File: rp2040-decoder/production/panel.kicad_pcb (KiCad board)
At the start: 4 copper layers, 70 x 70 mm, 535 parts, among them J4 5052702412, Q1 TPM2008, Q2 TPM2008, Q3 TPM2008, Q4 TPM2008, Q5 TPM2008, Q6 TPM2008, Q7 TPM2008, U1 W25Q64JVXGIQ, U2 AP63203WU, U3 RP2040, U4 MD9927, U5 MAX98357A, U6 LMV331, Y1 X252012MMB4SI

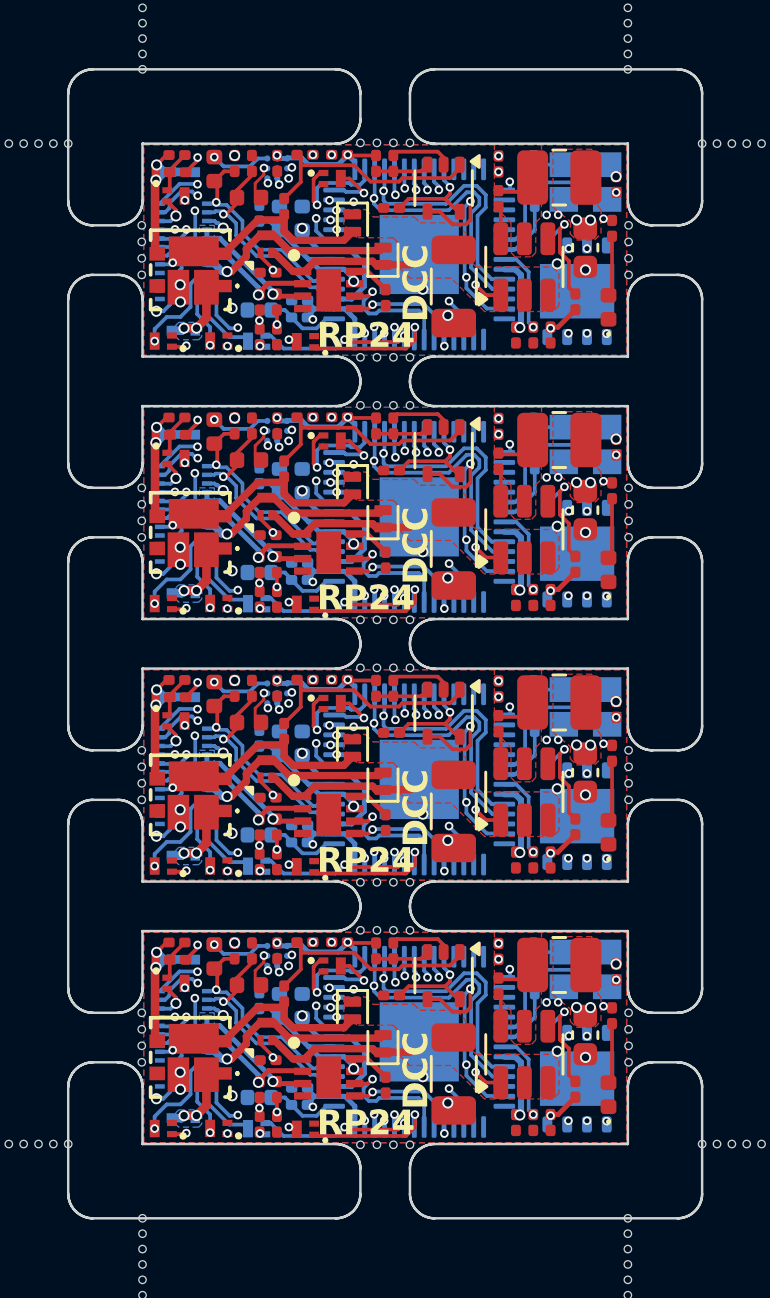
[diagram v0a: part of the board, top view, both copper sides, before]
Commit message: fix: convert 0.2mm vias to 0.3mm
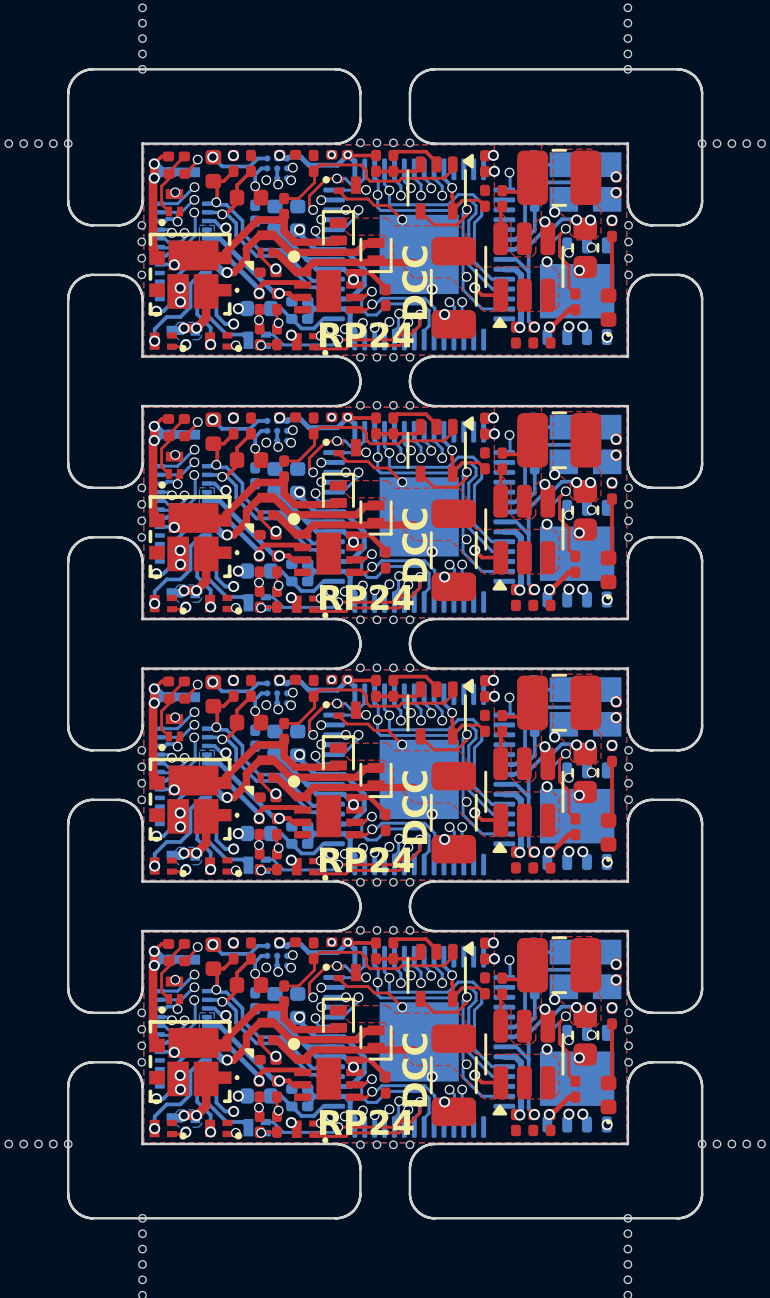
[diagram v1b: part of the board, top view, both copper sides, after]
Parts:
- removed the C10 at (144.2, 37.8)
- removed the C10 at (144.2, 59.0)
- removed the C10 at (144.2, 48.4)
- removed the C10 at (144.2, 69.6)
- removed the C11 at (145.0, 41.1)
- removed the C11 at (145.0, 72.9)
- removed the C11 at (145.0, 62.3)
- removed the C11 at (145.0, 51.7)
- removed the C12 at (143.4, 37.6)
- removed the C12 at (143.4, 58.8)
- removed the C12 at (143.4, 69.4)
- removed the C12 at (143.4, 48.2)
- removed the C14 at (143.4, 52.1)
- removed the C14 at (143.4, 41.5)
- removed the C14 at (143.4, 73.3)
- removed the C14 at (143.4, 62.7)
- removed the C15 at (143.8, 61.2)
- removed the C15 at (143.8, 40.0)
- removed the C15 at (143.8, 50.6)
- removed the C15 at (143.8, 71.8)
- removed the C17 at (153.1, 67.4)
- removed the C17 at (153.1, 35.6)
- removed the C17 at (153.1, 46.2)
- removed the C17 at (153.1, 56.8)
- removed the C18 at (151.3, 40.6)
- removed the C18 at (151.3, 72.4)
- removed the C18 at (151.3, 61.8)
- removed the C18 at (151.3, 51.2)
- removed the C20 at (143.1, 67.4)
- removed the C20 at (143.1, 46.2)
- removed the C20 at (143.1, 35.6)
- removed the C20 at (143.1, 56.8)
- removed the C21 at (144.1, 56.8)
- removed the C21 at (144.1, 67.4)
- removed the C21 at (144.1, 35.6)
- removed the C21 at (144.1, 46.2)
- removed the C22 at (142.4, 67.4)
- removed the C22 at (142.4, 46.2)
- removed the C22 at (142.4, 35.6)
- removed the C22 at (142.4, 56.8)
- removed the C3 at (157.8, 68.2)
- removed the C3 at (157.8, 36.5)
- removed the C3 at (157.8, 47.0)
- removed the C3 at (157.8, 57.6)
- removed the C5 at (148.8, 58.6)
- removed the C5 at (148.8, 37.4)
- removed the C5 at (148.8, 48.0)
- removed the C5 at (148.8, 69.2)
- removed the C6 at (153.1, 37.0)
- removed the C6 at (153.1, 47.6)
- removed the C6 at (153.1, 58.2)
- removed the C6 at (153.1, 68.8)
- removed the C8 at (145.2, 59.0)
- removed the C8 at (145.2, 37.8)
- removed the C8 at (145.2, 69.6)
- removed the C8 at (145.2, 48.4)
- removed the C9 at (156.6, 39.0)
- removed the C9 at (156.6, 49.6)
- removed the C9 at (156.6, 60.2)
- removed the C9 at (156.6, 70.8)
- removed the D1 at (140.6, 39.9)
- removed the D1 at (140.6, 61.1)
- removed the D1 at (140.6, 50.5)
- removed the D1 at (140.6, 71.7)
- removed the D2 at (157.5, 41.4)
- removed the D2 at (157.5, 52.0)
- removed the D2 at (157.5, 62.6)
- removed the D2 at (157.5, 73.2)
- removed the D3 at (148.4, 60.5)
- removed the D3 at (148.4, 39.4)
- removed the D3 at (148.4, 71.2)
- removed the D3 at (148.4, 50.0)
- removed the D4 at (147.2, 59.2)
- removed the D4 at (147.2, 38.0)
- removed the D4 at (147.2, 69.8)
- removed the D4 at (147.2, 48.6)
- removed the FB1 at (141.6, 46.4)
- removed the FB1 at (141.6, 67.6)
- removed the FB1 at (141.6, 35.8)
- removed the FB1 at (141.6, 57.0)
- removed the L1 at (155.5, 68.0)
- removed the L1 at (155.5, 57.4)
- removed the L1 at (155.5, 36.2)
- removed the L1 at (155.5, 46.8)
- removed the Q1 at (140.1, 68.7)
- removed the Q1 at (140.1, 47.5)
- removed the Q1 at (140.1, 58.1)
- removed the Q1 at (140.1, 36.9)
- removed the Q4 at (146.4, 36.2)
- removed the Q4 at (146.4, 68.0)
- removed the Q4 at (146.4, 46.8)
- removed the Q4 at (146.4, 57.4)
- removed the Q5 at (143.3, 53.4)
- removed the Q5 at (143.3, 42.8)
- removed the Q5 at (143.3, 64.0)
- removed the Q5 at (143.3, 74.6)
- removed the R1 at (140.1, 56.5)
- removed the R1 at (140.1, 67.1)
- removed the R1 at (140.1, 35.3)
- removed the R1 at (140.1, 45.9)
- removed the R10 at (145.0, 52.4)
- removed the R10 at (145.0, 41.8)
- removed the R10 at (145.0, 73.6)
- removed the R10 at (145.0, 63.0)
- removed the R11 at (143.4, 51.8)
- removed the R11 at (143.4, 73.0)
- removed the R11 at (143.4, 41.2)
- removed the R11 at (143.4, 62.4)
- removed the R13 at (144.1, 73.0)
- removed the R13 at (144.1, 62.4)
- removed the R13 at (144.1, 51.8)
- removed the R13 at (144.1, 41.2)
- removed the R2 at (140.1, 67.8)
- removed the R2 at (140.1, 46.6)
- removed the R2 at (140.1, 36.0)
- removed the R2 at (140.1, 57.2)
- removed the R4 at (145.3, 56.5)
- removed the R4 at (145.3, 35.2)
- removed the R4 at (145.3, 67.0)
- removed the R4 at (145.3, 45.9)
- removed the R9 at (157.7, 70.0)
- removed the R9 at (157.7, 38.2)
- removed the R9 at (157.7, 59.4)
- removed the R9 at (157.7, 48.8)
- removed the U4 at (146.2, 61.9)
- removed the U4 at (146.2, 40.7)
- removed the U4 at (146.2, 72.5)
- removed the U4 at (146.2, 51.3)
- removed the U6 at (150.9, 47.2)
- removed the U6 at (150.9, 68.4)
- removed the U6 at (150.9, 57.8)
- removed the U6 at (150.9, 36.6)
- added C10: 10uF, Capacitor_SMD:C_0402_1005Metric, B.Cu at (144.1, 69.6)
- added C10: 10uF, Capacitor_SMD:C_0402_1005Metric, B.Cu at (144.1, 59.0)
- added C10: 10uF, Capacitor_SMD:C_0402_1005Metric, B.Cu at (144.1, 48.4)
- added C10: 10uF, Capacitor_SMD:C_0402_1005Metric, B.Cu at (144.1, 37.8)
- added C11: 100nF, Capacitor_SMD:C_0201_0603Metric, B.Cu at (145.1, 51.8)
- added C11: 100nF, Capacitor_SMD:C_0201_0603Metric, B.Cu at (145.1, 41.2)
- added C11: 100nF, Capacitor_SMD:C_0201_0603Metric, B.Cu at (145.1, 62.4)
- added C11: 100nF, Capacitor_SMD:C_0201_0603Metric, B.Cu at (145.1, 73.0)
- added C12: 100nF, Capacitor_SMD:C_0201_0603Metric, B.Cu at (143.2, 69.4)
- added C12: 100nF, Capacitor_SMD:C_0201_0603Metric, B.Cu at (143.2, 48.2)
- added C12: 100nF, Capacitor_SMD:C_0201_0603Metric, B.Cu at (143.2, 58.8)
- added C12: 100nF, Capacitor_SMD:C_0201_0603Metric, B.Cu at (143.2, 37.6)
- added C14: 10uF, Capacitor_SMD:C_0402_1005Metric, B.Cu at (143.4, 41.5)
- added C14: 10uF, Capacitor_SMD:C_0402_1005Metric, B.Cu at (143.4, 62.7)
- added C14: 10uF, Capacitor_SMD:C_0402_1005Metric, B.Cu at (143.4, 52.1)
- added C14: 10uF, Capacitor_SMD:C_0402_1005Metric, B.Cu at (143.4, 73.3)
- added C15: 10pF, Capacitor_SMD:C_0201_0603Metric, F.Cu at (143.8, 50.6)
- added C15: 10pF, Capacitor_SMD:C_0201_0603Metric, F.Cu at (143.8, 61.2)
- added C15: 10pF, Capacitor_SMD:C_0201_0603Metric, F.Cu at (143.8, 40.0)
- added C15: 10pF, Capacitor_SMD:C_0201_0603Metric, F.Cu at (143.8, 71.8)
- added C17: 100nF, Capacitor_SMD:C_0201_0603Metric, F.Cu at (152.5, 67.4)
- added C17: 100nF, Capacitor_SMD:C_0201_0603Metric, F.Cu at (152.5, 35.6)
- added C17: 100nF, Capacitor_SMD:C_0201_0603Metric, F.Cu at (152.5, 46.2)
- added C17: 100nF, Capacitor_SMD:C_0201_0603Metric, F.Cu at (152.5, 56.8)
- added C18: 47uF, Capacitor_SMD:C_1206_3216Metric, F.Cu at (151.3, 72.4)
- added C18: 47uF, Capacitor_SMD:C_1206_3216Metric, F.Cu at (151.3, 40.6)
- added C18: 47uF, Capacitor_SMD:C_1206_3216Metric, F.Cu at (151.3, 51.2)
- added C18: 47uF, Capacitor_SMD:C_1206_3216Metric, F.Cu at (151.3, 61.8)
- added C20: 220pF, Capacitor_SMD:C_0201_0603Metric, F.Cu at (143.1, 46.2)
- added C20: 220pF, Capacitor_SMD:C_0201_0603Metric, F.Cu at (143.1, 35.6)
- added C20: 220pF, Capacitor_SMD:C_0201_0603Metric, F.Cu at (143.1, 56.8)
- added C20: 220pF, Capacitor_SMD:C_0201_0603Metric, F.Cu at (143.1, 67.4)
- added C21: 100nF, Capacitor_SMD:C_0201_0603Metric, F.Cu at (144.6, 45.9)
- added C21: 100nF, Capacitor_SMD:C_0201_0603Metric, F.Cu at (144.6, 56.5)
- added C21: 100nF, Capacitor_SMD:C_0201_0603Metric, F.Cu at (144.6, 67.0)
- added C21: 100nF, Capacitor_SMD:C_0201_0603Metric, F.Cu at (144.6, 35.2)
- added C22: 220pF, Capacitor_SMD:C_0201_0603Metric, F.Cu at (142.4, 67.4)
- added C22: 220pF, Capacitor_SMD:C_0201_0603Metric, F.Cu at (142.4, 56.8)
- added C22: 220pF, Capacitor_SMD:C_0201_0603Metric, F.Cu at (142.4, 35.6)
- added C22: 220pF, Capacitor_SMD:C_0201_0603Metric, F.Cu at (142.4, 46.2)
- added C3: 10pF, Capacitor_SMD:C_0201_0603Metric, F.Cu at (157.8, 68.3)
- added C3: 10pF, Capacitor_SMD:C_0201_0603Metric, F.Cu at (157.8, 36.5)
- added C3: 10pF, Capacitor_SMD:C_0201_0603Metric, F.Cu at (157.8, 57.7)
- added C3: 10pF, Capacitor_SMD:C_0201_0603Metric, F.Cu at (157.8, 47.1)
- added C5: 100nF, Capacitor_SMD:C_0201_0603Metric, F.Cu at (152.5, 37.0)
- added C5: 100nF, Capacitor_SMD:C_0201_0603Metric, F.Cu at (152.5, 68.8)
- added C5: 100nF, Capacitor_SMD:C_0201_0603Metric, F.Cu at (152.5, 58.2)
- added C5: 100nF, Capacitor_SMD:C_0201_0603Metric, F.Cu at (152.5, 47.6)
- added C6: 100nF, Capacitor_SMD:C_0201_0603Metric, F.Cu at (153.2, 37.0)
- added C6: 100nF, Capacitor_SMD:C_0201_0603Metric, F.Cu at (153.2, 58.2)
- added C6: 100nF, Capacitor_SMD:C_0201_0603Metric, F.Cu at (153.2, 68.8)
- added C6: 100nF, Capacitor_SMD:C_0201_0603Metric, F.Cu at (153.2, 47.6)
- added C8: 10uF, Capacitor_SMD:C_0402_1005Metric, B.Cu at (145.0, 37.8)
- added C8: 10uF, Capacitor_SMD:C_0402_1005Metric, B.Cu at (145.0, 59.0)
- added C8: 10uF, Capacitor_SMD:C_0402_1005Metric, B.Cu at (145.0, 48.4)
- added C8: 10uF, Capacitor_SMD:C_0402_1005Metric, B.Cu at (145.0, 69.6)
- added C9: 22uF, Capacitor_SMD:C_0603_1608Metric, F.Cu at (156.6, 70.8)
- added C9: 22uF, Capacitor_SMD:C_0603_1608Metric, F.Cu at (156.6, 60.2)
- added C9: 22uF, Capacitor_SMD:C_0603_1608Metric, F.Cu at (156.6, 49.6)
- added C9: 22uF, Capacitor_SMD:C_0603_1608Metric, F.Cu at (156.6, 39.0)
- added D1: NSR1030QMU, Local Library:NSR1030QMU, F.Cu at (140.6, 40.1)
- added D1: NSR1030QMU, Local Library:NSR1030QMU, F.Cu at (140.6, 61.3)
- added D1: NSR1030QMU, Local Library:NSR1030QMU, F.Cu at (140.6, 50.7)
- added D1: NSR1030QMU, Local Library:NSR1030QMU, F.Cu at (140.6, 71.9)
- added D2: Blue LED, LED_SMD:LED_0402_1005Metric, F.Cu at (157.5, 52.0)
- added D2: Blue LED, LED_SMD:LED_0402_1005Metric, F.Cu at (157.5, 41.4)
- added D2: Blue LED, LED_SMD:LED_0402_1005Metric, F.Cu at (157.5, 62.6)
- added D2: Blue LED, LED_SMD:LED_0402_1005Metric, F.Cu at (157.5, 73.2)
- added D3: PSBD2FD40V1H, Diode_SMD:D_SOD-882, F.Cu at (148.1, 71.0)
- added D3: PSBD2FD40V1H, Diode_SMD:D_SOD-882, F.Cu at (148.1, 60.4)
- added D3: PSBD2FD40V1H, Diode_SMD:D_SOD-882, F.Cu at (148.1, 39.2)
- added D3: PSBD2FD40V1H, Diode_SMD:D_SOD-882, F.Cu at (148.1, 49.8)
- added D4: PSBD2FD40V1H, Diode_SMD:D_SOD-882, F.Cu at (146.6, 38.4)
- added D4: PSBD2FD40V1H, Diode_SMD:D_SOD-882, F.Cu at (146.6, 59.6)
- added D4: PSBD2FD40V1H, Diode_SMD:D_SOD-882, F.Cu at (146.6, 49.0)
- added D4: PSBD2FD40V1H, Diode_SMD:D_SOD-882, F.Cu at (146.6, 70.2)
- added FB1: FB_P, Inductor_SMD:L_0402_1005Metric, F.Cu at (141.6, 57.0)
- added FB1: FB_P, Inductor_SMD:L_0402_1005Metric, F.Cu at (141.6, 67.6)
- added FB1: FB_P, Inductor_SMD:L_0402_1005Metric, F.Cu at (141.6, 46.4)
- added FB1: FB_P, Inductor_SMD:L_0402_1005Metric, F.Cu at (141.6, 35.8)
- added L1: 4.7uH, Inductor_SMD:L_1008_2520Metric, F.Cu at (155.5, 36.2)
- added L1: 4.7uH, Inductor_SMD:L_1008_2520Metric, F.Cu at (155.5, 68.0)
- added L1: 4.7uH, Inductor_SMD:L_1008_2520Metric, F.Cu at (155.5, 57.4)
- added L1: 4.7uH, Inductor_SMD:L_1008_2520Metric, F.Cu at (155.5, 46.8)
- added Q1: TPM2008, Local Library:Diodes_DFN1006-3, F.Cu at (140.0, 58.4)
- added Q1: TPM2008, Local Library:Diodes_DFN1006-3, F.Cu at (140.0, 37.2)
- added Q1: TPM2008, Local Library:Diodes_DFN1006-3, F.Cu at (140.0, 69.0)
- added Q1: TPM2008, Local Library:Diodes_DFN1006-3, F.Cu at (140.0, 47.8)
- added Q4: TPM2008, Local Library:Diodes_DFN1006-3, F.Cu at (147.0, 57.7)
- added Q4: TPM2008, Local Library:Diodes_DFN1006-3, F.Cu at (147.0, 68.3)
- added Q4: TPM2008, Local Library:Diodes_DFN1006-3, F.Cu at (147.0, 47.1)
- added Q4: TPM2008, Local Library:Diodes_DFN1006-3, F.Cu at (147.0, 36.5)
- added Q5: TPM2008, Local Library:Diodes_DFN1006-3, B.Cu at (143.3, 53.3)
- added Q5: TPM2008, Local Library:Diodes_DFN1006-3, B.Cu at (143.3, 63.9)
- added Q5: TPM2008, Local Library:Diodes_DFN1006-3, B.Cu at (143.3, 74.5)
- added Q5: TPM2008, Local Library:Diodes_DFN1006-3, B.Cu at (143.3, 42.7)
- added R1: 6.8K, Resistor_SMD:R_0201_0603Metric, F.Cu at (140.1, 35.3)
- added R1: 6.8K, Resistor_SMD:R_0201_0603Metric, F.Cu at (140.1, 56.5)
- added R1: 6.8K, Resistor_SMD:R_0201_0603Metric, F.Cu at (140.1, 45.9)
- added R1: 6.8K, Resistor_SMD:R_0201_0603Metric, F.Cu at (140.1, 67.1)
- added R10: 200R, Resistor_SMD:R_0201_0603Metric, B.Cu at (145.1, 63.1)
- added R10: 200R, Resistor_SMD:R_0201_0603Metric, B.Cu at (145.1, 52.5)
- added R10: 200R, Resistor_SMD:R_0201_0603Metric, B.Cu at (145.1, 41.9)
- added R10: 200R, Resistor_SMD:R_0201_0603Metric, B.Cu at (145.1, 73.7)
- added R11: 6.8K, Resistor_SMD:R_0201_0603Metric, F.Cu at (143.4, 62.4)
- added R11: 6.8K, Resistor_SMD:R_0201_0603Metric, F.Cu at (143.4, 73.0)
- added R11: 6.8K, Resistor_SMD:R_0201_0603Metric, F.Cu at (143.4, 41.2)
- added R11: 6.8K, Resistor_SMD:R_0201_0603Metric, F.Cu at (143.4, 51.8)
- added R13: 6.8K, Resistor_SMD:R_0201_0603Metric, F.Cu at (144.1, 73.0)
- added R13: 6.8K, Resistor_SMD:R_0201_0603Metric, F.Cu at (144.1, 62.4)
- added R13: 6.8K, Resistor_SMD:R_0201_0603Metric, F.Cu at (144.1, 41.2)
- added R13: 6.8K, Resistor_SMD:R_0201_0603Metric, F.Cu at (144.1, 51.8)
- added R2: 6.8K, Resistor_SMD:R_0201_0603Metric, F.Cu at (140.1, 57.2)
- added R2: 6.8K, Resistor_SMD:R_0201_0603Metric, F.Cu at (140.1, 46.6)
- added R2: 6.8K, Resistor_SMD:R_0201_0603Metric, F.Cu at (140.1, 67.8)
- added R2: 6.8K, Resistor_SMD:R_0201_0603Metric, F.Cu at (140.1, 36.0)
- added R4: 33K, Resistor_SMD:R_0201_0603Metric, F.Cu at (145.6, 46.2)
- added R4: 33K, Resistor_SMD:R_0201_0603Metric, F.Cu at (145.6, 35.6)
- added R4: 33K, Resistor_SMD:R_0201_0603Metric, F.Cu at (145.6, 67.4)
- added R4: 33K, Resistor_SMD:R_0201_0603Metric, F.Cu at (145.6, 56.8)
- added R9: 1K, Resistor_SMD:R_0201_0603Metric, F.Cu at (157.7, 59.4)
- added R9: 1K, Resistor_SMD:R_0201_0603Metric, F.Cu at (157.7, 70.0)
- added R9: 1K, Resistor_SMD:R_0201_0603Metric, F.Cu at (157.7, 38.2)
- added R9: 1K, Resistor_SMD:R_0201_0603Metric, F.Cu at (157.7, 48.8)
- added U4: MD9927, Local Library:LM293QT, F.Cu at (146.2, 62.0)
- added U4: MD9927, Local Library:LM293QT, F.Cu at (146.2, 51.4)
- added U4: MD9927, Local Library:LM293QT, F.Cu at (146.2, 72.6)
- added U4: MD9927, Local Library:LM293QT, F.Cu at (146.2, 40.8)
- added U6: LMV331, Package_TO_SOT_SMD:SOT-353_SC-70-5, F.Cu at (150.6, 57.8)
- added U6: LMV331, Package_TO_SOT_SMD:SOT-353_SC-70-5, F.Cu at (150.6, 47.2)
- added U6: LMV331, Package_TO_SOT_SMD:SOT-353_SC-70-5, F.Cu at (150.6, 36.6)
- added U6: LMV331, Package_TO_SOT_SMD:SOT-353_SC-70-5, F.Cu at (150.6, 68.4)
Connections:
- U5 pad B2: Board_1-unconnected-(U5-GAIN_SLOT-PadB2) -> Board_1-GND
- U5 pad B2: Board_2-unconnected-(U5-GAIN_SLOT-PadB2) -> Board_2-GND
- U5 pad B2: Board_0-unconnected-(U5-GAIN_SLOT-PadB2) -> Board_0-GND
- U5 pad B2: Board_3-unconnected-(U5-GAIN_SLOT-PadB2) -> Board_3-GND
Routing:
- net Board_0-GND: track 5.86 -> 10.1 mm, vias 20 -> 21
- net Board_2-GND: track 5.86 -> 10.1 mm, vias 20 -> 21
- net Board_3-GND: track 5.86 -> 10.1 mm, vias 20 -> 21
- net Board_1-GND: track 5.86 -> 10.1 mm, vias 20 -> 21
- net Board_2-Net-(U1-IO3): track 11.8 -> 15.9 mm
- net Board_0-Net-(U1-IO3): track 11.8 -> 15.9 mm
- net Board_1-Net-(U1-IO3): track 11.8 -> 15.9 mm
- net Board_3-Net-(U1-IO3): track 11.8 -> 15.9 mm
- net Board_1-/AUX10: track 13.5 -> 11.7 mm, vias 2 -> 3
- net Board_3-/AUX10: track 13.5 -> 11.7 mm, vias 2 -> 3
- net Board_0-/AUX10: track 13.5 -> 11.7 mm, vias 2 -> 3
- net Board_2-/AUX10: track 13.5 -> 11.7 mm, vias 2 -> 3
- net Board_3-Net-(U1-IO2): track 19.4 -> 18.2 mm
- net Board_1-Net-(U1-IO2): track 19.4 -> 18.2 mm
- net Board_2-Net-(U1-IO2): track 19.4 -> 18.2 mm
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
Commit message: fix: reduce unique part count
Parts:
- R16 (x4): value 20K -> 4.7K
- R17 (x4): value 33K -> 6.8K
- R3 (x4): value 100K -> 6.8K
- R4 (x4): value 33K -> 2.2K
